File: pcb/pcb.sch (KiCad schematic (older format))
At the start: 0 parts

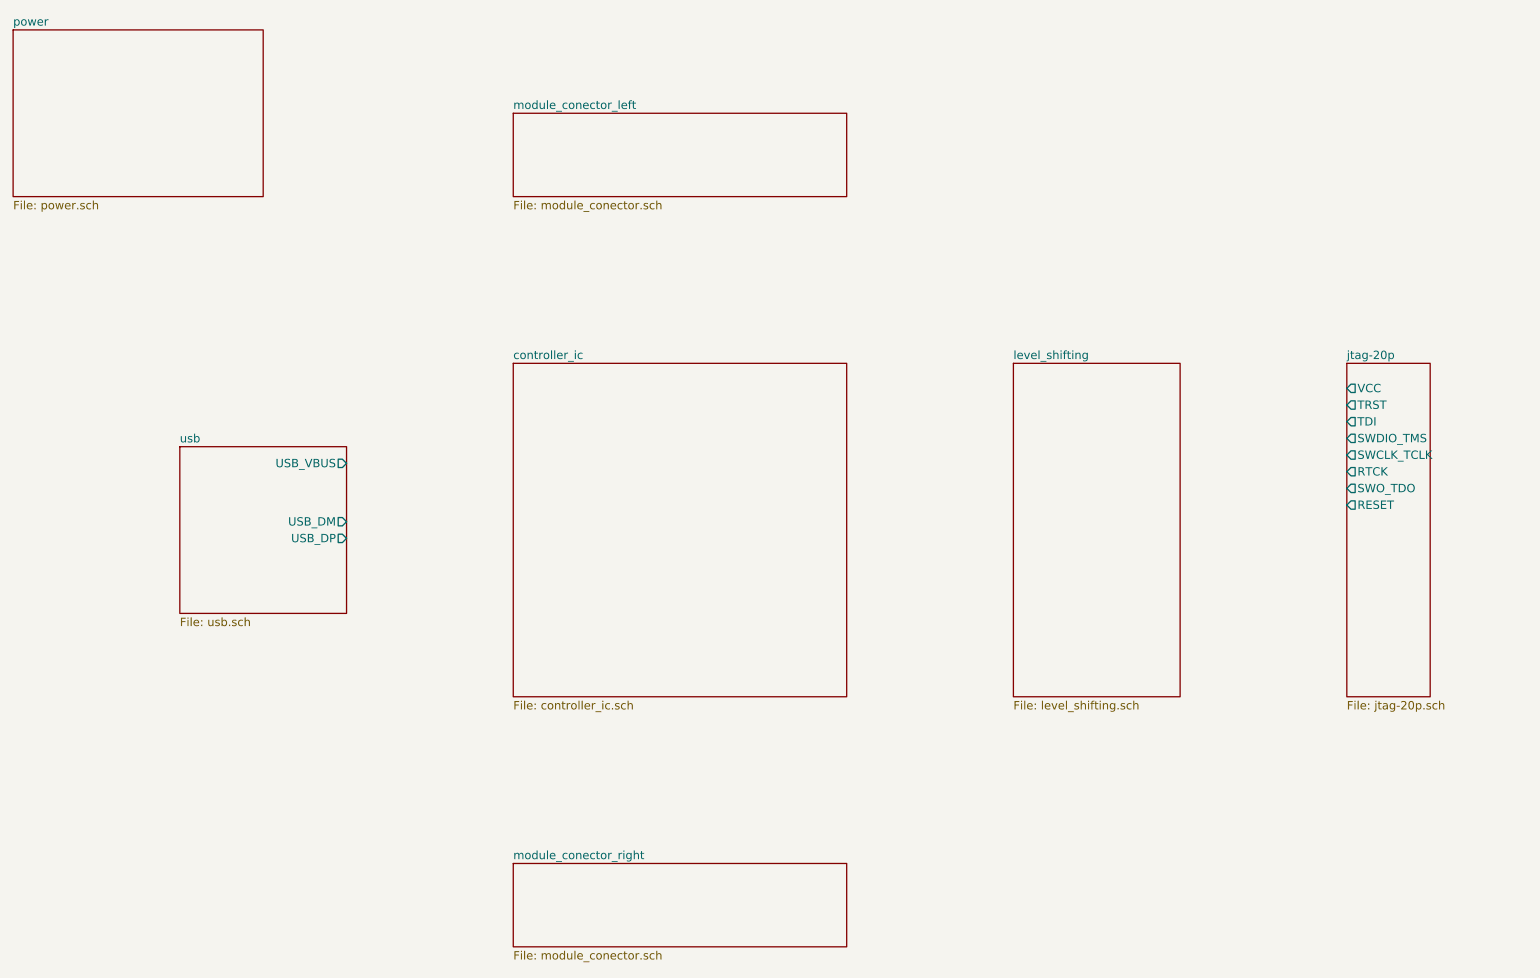
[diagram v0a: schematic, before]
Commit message: SCH: missing signal logic and level shifting
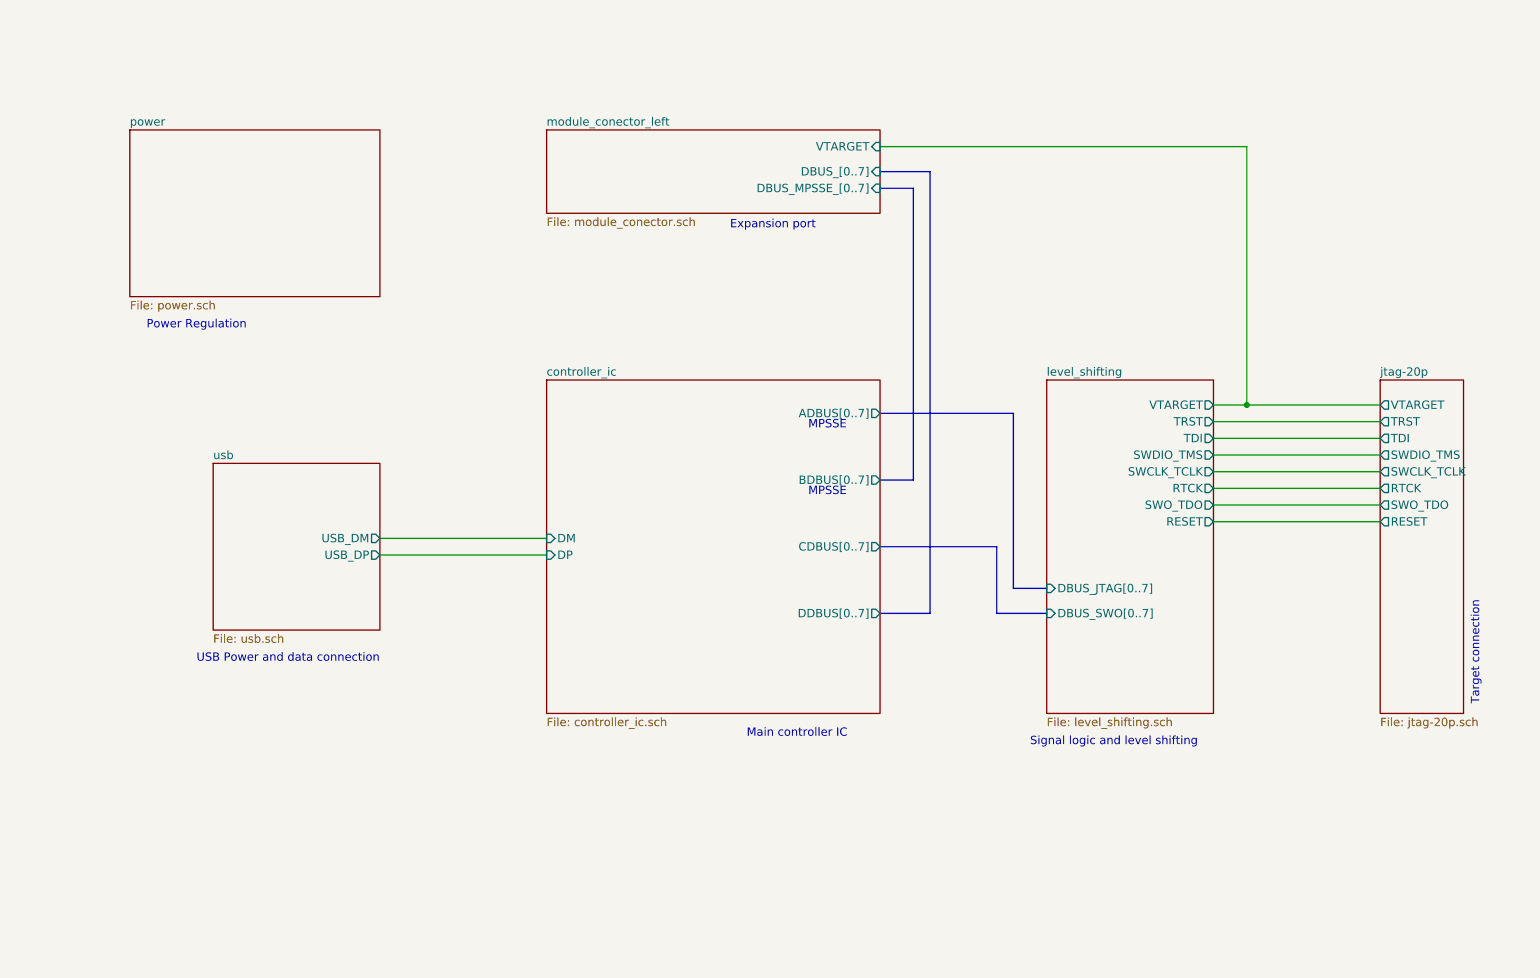
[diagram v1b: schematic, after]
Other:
- note added: "Expansion port"
- note added: "MPSSE"
- note added: "Main controller IC"
- note added: "Power Regulation"
- note added: "Signal logic and level shifting"
- note added: "Target connection"
- note added: "USB Power and data connection"
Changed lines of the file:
@@
 $Descr A4 11693 8268
 encoding utf-8
-Sheet 1 8
+Sheet 1 7
 Title "Modular-programmer"
 Date "2020-03-03"
@@
 $EndDescr
 $Sheet
-S 2000 3500 1000 1000
-U 5E60D30B
-F0 "usb" 50
-F1 "usb.sch" 50
-F2 "USB_DM" O R 3000 3950 50
-F3 "USB_DP" O R 3000 4050 50
-F4 "USB_VBUS" O R 3000 3600 50
-$EndSheet
-$Sheet
-S 4000 3000 2000 2000
+S 4200 3100 2000 2000
 U 5E60D352
 F0 "controller_ic" 50
 F1 "controller_ic.sch" 50
+F2 "ADBUS[0..7]" O R 6200 3300 50
+F3 "BDBUS[0..7]" O R 6200 3700 50
+F4 "CDBUS[0..7]" O R 6200 4100 50
+F5 "DDBUS[0..7]" O R 6200 4500 50
+F6 "DP" I L 4200 4150 50
+F7 "DM" I L 4200 4050 50
 $EndSheet
 $Sheet
-S 7000 3000 1000 2000
+S 7200 3100 1000 2000
 U 5E60D389
 F0 "level_shifting" 50
 F1 "level_shifting.sch" 50
+F2 "VTARGET" O R 8200 3250 50
+F3 "TRST" O R 8200 3350 50
+F4 "TDI" O R 8200 3450 50
+F5 "SWDIO_TMS" O R 8200 3550 50
+F6 "SWCLK_TCLK" O R 8200 3650 50
+F7 "RTCK" O R 8200 3750 50
+F8 "SWO_TDO" O R 8200 3850 50
+F9 "RESET" O R 8200 3950 50
+F10 "DBUS_SWO[0..7]" I L 7200 4500 50
+F11 "DBUS_JTAG[0..7]" I L 7200 4350 50
 $EndSheet
 $Sheet
-S 9000 3000 500  2000
+S 9200 3100 500  2000
 U 5E60D3C8
 F0 "jtag-20p" 50
 F1 "jtag-20p.sch" 50
-F2 "VCC" O L 9000 3150 50
-F3 "TRST" O L 9000 3250 50
-F4 "TDI" O L 9000 3350 50
-F5 "SWDIO_TMS" O L 9000 3450 50
-F6 "SWCLK_TCLK" O L 9000 3550 50
-F7 "RTCK" O L 9000 3650 50
-F8 "SWO_TDO" O L 9000 3750 50
-F9 "RESET" O L 9000 3850 50
+F2 "TRST" O L 9200 3350 50
+F3 "TDI" O L 9200 3450 50
+F4 "SWDIO_TMS" O L 9200 3550 50
+F5 "SWCLK_TCLK" O L 9200 3650 50
+F6 "RTCK" O L 9200 3750 50
+F7 "SWO_TDO" O L 9200 3850 50
+F8 "RESET" O L 9200 3950 50
+F9 "VTARGET" O L 9200 3250 50
 $EndSheet
 $Sheet
-S 4000 6000 2000 500
-U 5E60D41E
-F0 "module_conector_right" 50
-F1 "module_conector.sch" 50
-$EndSheet
-$Sheet
-S 4000 1500 2000 500
-U 5E60D4D7
-F0 "module_conector_left" 50
-F1 "module_conector.sch" 50
-$EndSheet
-$Sheet
-S 1000 1000 1500 1000
+S 1700 1600 1500 1000
 U 5E60EE3D
 F0 "power" 50
 F1 "power.sch" 50
 $EndSheet
+$Sheet
+S 2200 3600 1000 1000
+U 5E60D30B
+F0 "usb" 50
+F1 "usb.sch" 50
+F2 "USB_DM" O R 3200 4050 50
+F3 "USB_DP" O R 3200 4150 50
+$EndSheet
+Wire Wire Line
+	3200 4050 4200 4050
+Wire Wire Line
+	3200 4150 4200 4150
+Wire Wire Line
+	8200 3950 9200 3950
+Wire Wire Line
+	9200 3850 8200 3850
+Wire Wire Line
+	8200 3750 9200 3750
+Wire Wire Line
+	9200 3650 8200 3650
+Wire Wire Line
+	8200 3550 9200 3550
+Wire Wire Line
+	9200 3450 8200 3450
+Wire Wire Line
+	8200 3350 9200 3350
+Wire Wire Line
+	9200 3250 8400 3250
+Wire Wire Line
+	8400 3250 8400 1700
+Wire Wire Line
+	8400 1700 6200 1700
+Connection ~ 8400 3250
+Wire Wire Line
+	8400 3250 8200 3250
+Text Notes 6000 3400 2    50   ~ 0
+MPSSE
+Text Notes 6000 3800 2    50   ~ 0
+MPSSE
+Wire Bus Line
+	7200 4350 7000 4350
+Wire Bus Line
+	7000 4350 7000 3300
+Wire Bus Line
+	7000 3300 6200 3300
+Wire Bus Line
+	7200 4500 6900 4500
+Wire Bus Line
+	6900 4500 6900 4100
+Wire Bus Line
+	6900 4100 6200 4100
+$Sheet
+S 4200 1600 2000 500
+U 5E60D4D7
+F0 "module_conector_left" 50
+F1 "module_conector.sch" 50
+F2 "VTARGET" I R 6200 1700 50
+F3 "DBUS_MPSSE_[0..7]" I R 6200 1950 50
+F4 "DBUS_[0..7]" I R 6200 1850 50
+$EndSheet
+Wire Bus Line
+	6200 3700 6400 3700
+Wire Bus Line
+	6400 3700 6400 1950
+Wire Bus Line
+	6400 1950 6200 1950
+Wire Bus Line
+	6200 4500 6500 4500
+Wire Bus Line
+	6500 4500 6500 1850
+Wire Bus Line
+	6500 1850 6200 1850
+Text Notes 9800 5050 1    50   ~ 0
+Target connection
+Text Notes 7100 5300 0    50   ~ 0
+Signal logic and level shifting
+Text Notes 5400 5250 0    50   ~ 0
+Main controller IC
+Text Notes 2100 4800 0    50   ~ 0
+USB Power and data connection
+Text Notes 1800 2800 0    50   ~ 0
+Power Regulation
+Text Notes 5300 2200 0    50   ~ 0
+Expansion port
 $EndSCHEMATC
